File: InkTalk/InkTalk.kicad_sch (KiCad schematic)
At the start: 66 parts, among them J1 USB_C_Receptacle_USB2.0_14P, J4 Conn_ARM_SWD_TagConnect_TC2030, U1 Winbond W25Q16JVUXIQ, U2 LM1117, U3 RP2040, U4 SN65HVD1473DGSR, U5 SN65HVD1473DGSR, X1 12MHz

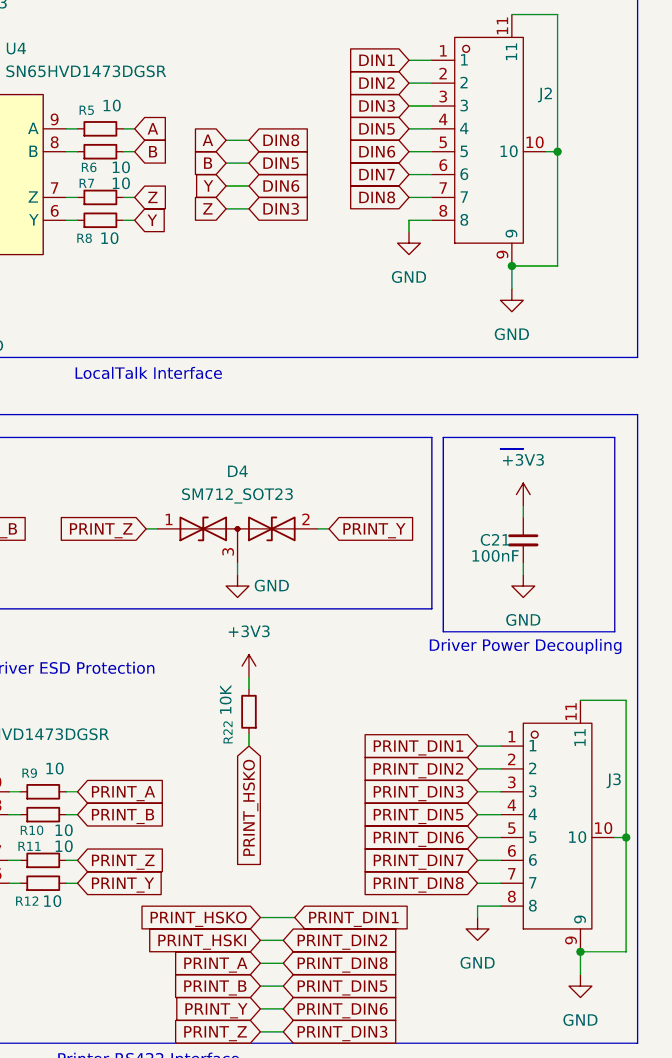
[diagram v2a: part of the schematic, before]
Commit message: Fix InkTalk and TashTalk USB flipped DIN pins
I accidentally transposed DIN7 and DIN8 when wiring up the connector
in KiCAD (yay weird pin choices on connectors). This explains the rather
odd and unexplainable cases of TashTalk USB not liking resistor pins
on PhoneNET connectors and long cables. It additionally caused InkTalk
to not work at all with the Colour StyleWriter 2200.

Easy fix thankfullly - commit contains just that flip around and some
minor board clean up for the first production-ish run of InkTalk.
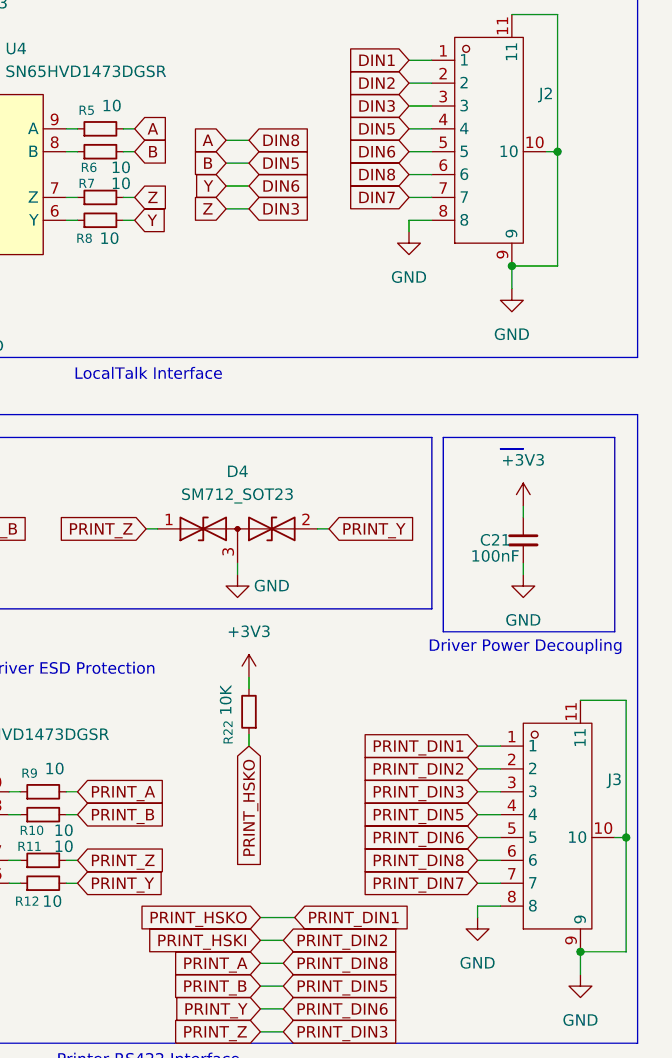
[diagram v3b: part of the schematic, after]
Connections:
- net A: now also J2.6; no longer J2.7
- net DIN7: now also J2.7; no longer J2.6
- net PRINT_A: now also J3.6; no longer J3.7
- net PRINT_DIN7: now also J3.7; no longer J3.6
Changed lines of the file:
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@@
 	(wire
 		(pts
+			(xy 255.27 63.5) (xy 257.81 63.5)
+		)
+		(stroke
+			(width 0)
+			(type default)
+		)
+	)
+	(wire
+		(pts
 			(xy 86.36 30.48) (xy 86.36 31.75)
 		)
@@
 	(wire
 		(pts
+			(xy 255.27 66.04) (xy 257.81 66.04)
+		)
+		(stroke
+			(width 0)
+			(type default)
+		)
+	)
+	(wire
+		(pts
 			(xy 105.41 21.59) (xy 105.41 20.32)
 		)
@@
 	(wire
 		(pts
-			(xy 262.89 142.24) (xy 265.43 142.24)
-		)
-		(stroke
-			(width 0)
-			(type default)
-		)
-	)
-	(wire
-		(pts
 			(xy 25.4 130.81) (xy 27.94 130.81)
 		)
@@
 	(wire
 		(pts
-			(xy 255.27 66.04) (xy 257.81 66.04)
-		)
-		(stroke
-			(width 0)
-			(type default)
-		)
-	)
-	(wire
-		(pts
 			(xy 210.82 26.67) (xy 212.09 26.67)
 		)
@@
 	(wire
 		(pts
+			(xy 262.89 139.7) (xy 265.43 139.7)
+		)
+		(stroke
+			(width 0)
+			(type default)
+		)
+	)
+	(wire
+		(pts
 			(xy 274.32 121.92) (xy 279.4 121.92)
 		)
@@
 	(wire
 		(pts
-			(xy 255.27 63.5) (xy 257.81 63.5)
-		)
-		(stroke
-			(width 0)
-			(type default)
-		)
-	)
-	(wire
-		(pts
 			(xy 127 27.94) (xy 127 30.48)
 		)
@@
 	(wire
 		(pts
-			(xy 262.89 139.7) (xy 265.43 139.7)
-		)
-		(stroke
-			(width 0)
-			(type default)
-		)
-	)
-	(wire
-		(pts
 			(xy 137.16 149.86) (xy 138.43 149.86)
 		)
@@
 	(wire
 		(pts
+			(xy 262.89 142.24) (xy 265.43 142.24)
+		)
+		(stroke
+			(width 0)
+			(type default)
+		)
+	)
+	(wire
+		(pts
 			(xy 223.52 58.42) (xy 224.79 58.42)
 		)
@@
 	(global_label "PRINT_DIN7"
 		(shape input)
-		(at 262.89 139.7 180)
+		(at 262.89 142.24 180)
 		(fields_autoplaced yes)
 		(effects
@@
 		)
 		(property "Intersheetrefs" "${INTERSHEET_REFS}"
-			(at 249.0795 139.7 0)
+			(at 249.0795 142.24 0)
 			(hide yes)
 			(show_name no)
@@
 	(global_label "DIN7"
 		(shape input)
-		(at 255.27 63.5 180)
+		(at 255.27 66.04 180)
 		(fields_autoplaced yes)
 		(effects
@@
 		)
 		(property "Intersheetrefs" "${INTERSHEET_REFS}"
-			(at 247.87 63.5 0)
+			(at 247.87 66.04 0)
 			(hide yes)
 			(show_name no)
@@
 	(global_label "DIN8"
 		(shape input)
-		(at 255.27 66.04 180)
+		(at 255.27 63.5 180)
 		(fields_autoplaced yes)
 		(effects
@@
 		)
 		(property "Intersheetrefs" "${INTERSHEET_REFS}"
-			(at 247.87 66.04 0)
+			(at 247.87 63.5 0)
 			(hide yes)
 			(show_name no)
@@
 	(global_label "PRINT_DIN8"
 		(shape input)
-		(at 262.89 142.24 180)
+		(at 262.89 139.7 180)
 		(fields_autoplaced yes)
 		(effects
@@
 		)
 		(property "Intersheetrefs" "${INTERSHEET_REFS}"
-			(at 249.0795 142.24 0)
+			(at 249.0795 139.7 0)
 			(hide yes)
 			(show_name no)

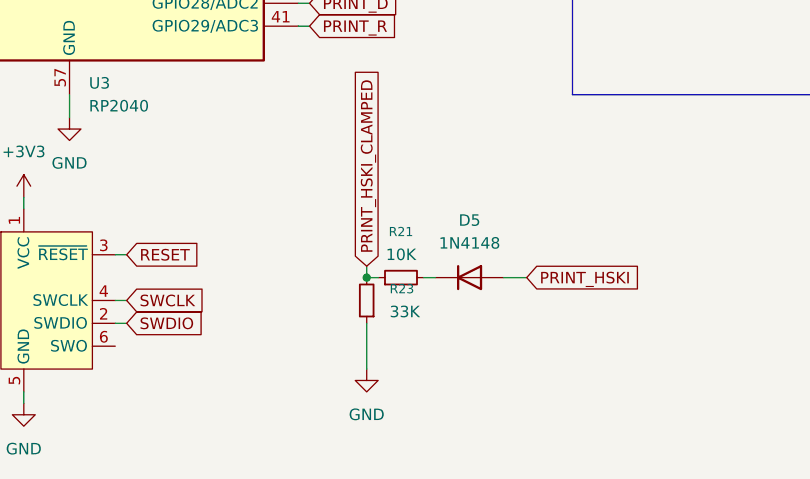
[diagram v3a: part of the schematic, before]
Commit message: InkTalk: Production ready tweaks
Handful of last changes I did before I sent the order off for production
yesterday. I changed the 10K / 33K combo for HSKi to 1K / 3K3 so we
could potentially use it for external clock mode, and then a few parts
updates like changing to Microchip's 3V3 reg, and assigning the right
LCSC part for D5.
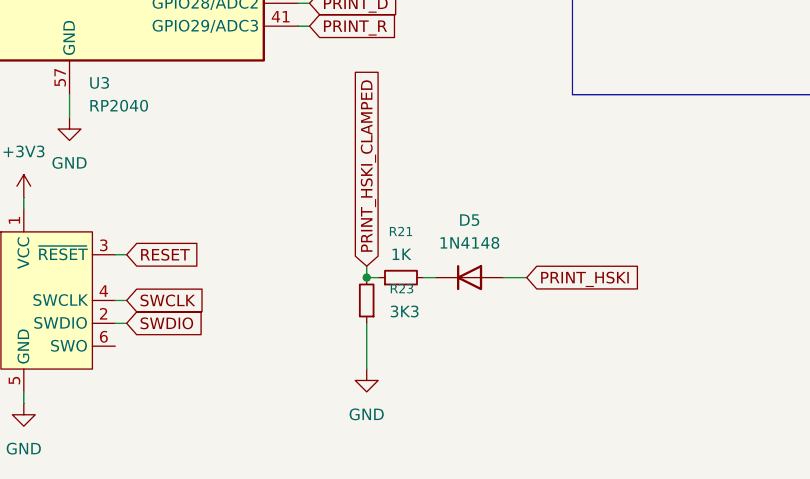
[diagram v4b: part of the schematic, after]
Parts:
- R21: value 10K -> 1K
- R23: value 33K -> 3K3
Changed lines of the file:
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@@
 			)
 		)
-		(property "Value" "33K"
+		(property "Value" "3K3"
 			(at 147.32 184.1499 0)
 			(show_name no)
@@
 			)
 		)
-		(property "Value" "10K"
+		(property "Value" "1K"
 			(at 148.59 177.8 90)
 			(show_name no)
